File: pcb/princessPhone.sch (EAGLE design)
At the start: 78 parts, among them P1 TC2030-MCP-NL, P2 10118194, P3 95009-7441, Q1 2N7002K, U1 Value, U2 AG1170-S3-VERTICAL, U3 PI32MX170D-PT, U4 BLUETOOTH-RN-52

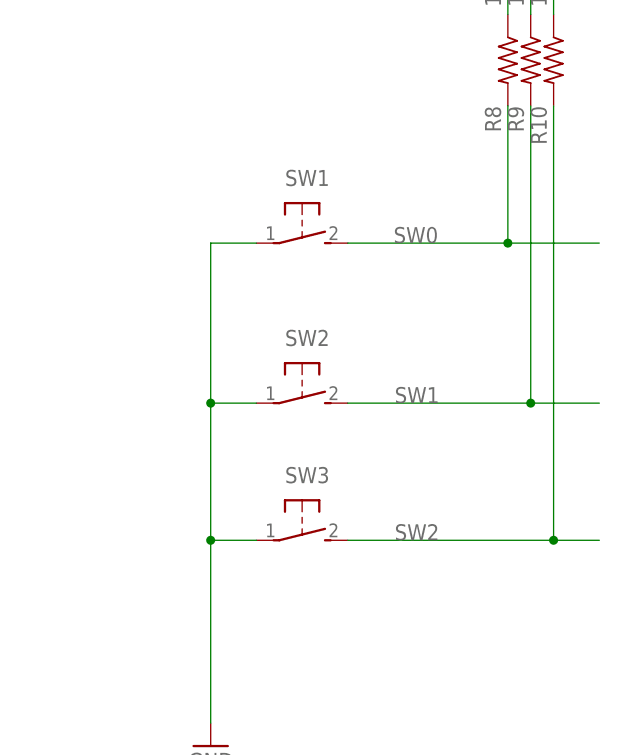
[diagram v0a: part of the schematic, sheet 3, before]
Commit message: Replaced placeholder components with proper ones.
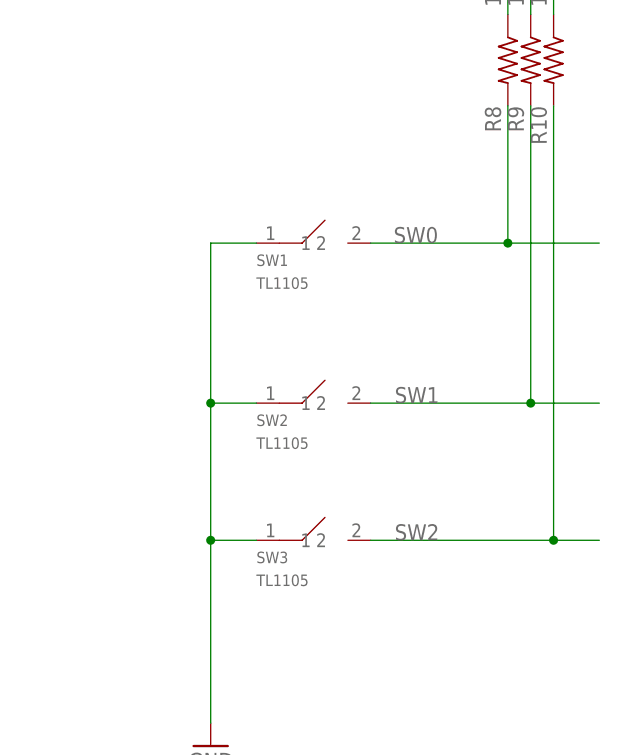
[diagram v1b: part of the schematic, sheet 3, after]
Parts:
- C1, C3: device rcl:CPOL-US153CLV-0505 -> rcl:CPOL-USE2.5-7
- SW1, SW2, SW3: value (none) -> TL1105; device switch-omron:31-XX -> princessPhone:TL1105
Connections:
- net GND: now also SW1.1, SW2.1, SW3.1; no longer SW1.P, SW2.P, SW3.P
- net SW0: now also SW1.2; no longer SW1.S
- net SW1: now also SW2.2; no longer SW2.S
- net SW2: now also SW3.2; no longer SW3.S
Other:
- note added: "2015.08.10"
- note added: "CORRECTED A FEW DRC ERRORS, REPLACED BIG CAPS AND BUTTONS"
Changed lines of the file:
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@@
 <part name="+3V31" library="supply1" deviceset="+3V3" device=""/>
 <part name="GND1" library="supply1" deviceset="GND" device=""/>
-<part name="C1" library="rcl" deviceset="CPOL-US" device="153CLV-0505" value="220UF"/>
+<part name="C1" library="rcl" deviceset="CPOL-US" device="E2.5-7" value="220UF"/>
 <part name="C2" library="rcl" deviceset="C-US" device="C0603" value="0.1UF"/>
 <part name="R1" library="rcl" deviceset="R-US_" device="R0603" value="2"/>
-<part name="C3" library="rcl" deviceset="CPOL-US" device="153CLV-0505" value="100UF"/>
+<part name="C3" library="rcl" deviceset="CPOL-US" device="E2.5-7" value="100UF"/>
 <part name="C4" library="rcl" deviceset="C-US" device="C0603" value="0.1UF"/>
 <part name="R2" library="rcl" deviceset="R-US_" device="R0603" value="1K"/>
@@
 <part name="LED4" library="led" deviceset="LED" device="CHIPLED_0603" value="BLUE"/>
 <part name="R29" library="rcl" deviceset="R-US_" device="R0603" value="150"/>
-<part name="SW1" library="switch-omron" deviceset="31-XX" device=""/>
-<part name="SW2" library="switch-omron" deviceset="31-XX" device=""/>
-<part name="SW3" library="switch-omron" deviceset="31-XX" device=""/>
 <part name="P2" library="console_board" deviceset="10118194" device=""/>
 <part name="P3" library="princessPhone" deviceset="95009-7441" device=""/>
+<part name="SW1" library="princessPhone" deviceset="TL1105*" device=""/>
+<part name="SW2" library="princessPhone" deviceset="TL1105*" device=""/>
+<part name="SW3" library="princessPhone" deviceset="TL1105*" device=""/>
 </parts>
 <sheets>
@@
 <text x="144.78" y="165.1" size="2.54" layer="94">2015.08.09</text>
 <text x="193.04" y="165.1" size="2.54" layer="94">FINISHED ROUTING, UPDATED USB/RJ-11/BOARD OUTLINE</text>
+<text x="50.8" y="160.02" size="2.54" layer="94">ANDERS NELSON</text>
+<text x="144.78" y="160.02" size="2.54" layer="94">2015.08.10</text>
+<text x="193.04" y="154.94" size="2.54" layer="94">CORRECTED A FEW DRC ERRORS,
+REPLACED BIG CAPS AND BUTTONS</text>
 </plain>
 <instances>
@@
 <attribute name="VALUE" x="149.86" y="33.02" size="1.778" layer="96"/>
 </instance>
-<instance part="SW1" gate="1" x="322.58" y="149.86" rot="R270"/>
-<instance part="SW2" gate="1" x="322.58" y="132.08" rot="R270"/>
-<instance part="SW3" gate="1" x="322.58" y="116.84" rot="R270"/>
+<instance part="SW1" gate="G$1" x="322.58" y="149.86"/>
+<instance part="SW2" gate="G$1" x="322.58" y="132.08"/>
+<instance part="SW3" gate="G$1" x="322.58" y="116.84"/>
 </instances>
 <busses>
@@
 <junction x="312.42" y="132.08"/>
 <pinref part="GND6" gate="1" pin="GND"/>
-<pinref part="SW1" gate="1" pin="P"/>
-<pinref part="SW2" gate="1" pin="P"/>
-<pinref part="SW3" gate="1" pin="P"/>
+<pinref part="SW1" gate="G$1" pin="1"/>
+<pinref part="SW2" gate="G$1" pin="1"/>
+<pinref part="SW3" gate="G$1" pin="1"/>
 </segment>
 </net>
@@
 <net name="SW0" class="0">
 <segment>
-<wire x1="327.66" y1="149.86" x2="345.44" y2="149.86" width="0.1524" layer="91"/>
+<wire x1="330.2" y1="149.86" x2="345.44" y2="149.86" width="0.1524" layer="91"/>
 <wire x1="345.44" y1="149.86" x2="355.6" y2="149.86" width="0.1524" layer="91"/>
 <wire x1="345.44" y1="165.1" x2="345.44" y2="149.86" width="0.1524" layer="91"/>
@@
 <label x="332.74" y="149.86" size="1.778" layer="95"/>
 <pinref part="R8" gate="G$1" pin="2"/>
-<pinref part="SW1" gate="1" pin="S"/>
+<pinref part="SW1" gate="G$1" pin="2"/>
 </segment>
 <segment>
@@
 <net name="SW1" class="0">
 <segment>
-<wire x1="327.66" y1="132.08" x2="347.98" y2="132.08" width="0.1524" layer="91"/>
+<wire x1="330.2" y1="132.08" x2="347.98" y2="132.08" width="0.1524" layer="91"/>
 <wire x1="347.98" y1="132.08" x2="355.6" y2="132.08" width="0.1524" layer="91"/>
 <wire x1="347.98" y1="165.1" x2="347.98" y2="132.08" width="0.1524" layer="91"/>
@@
 <label x="337.82" y="132.08" size="1.778" layer="95" rot="MR0"/>
 <pinref part="R9" gate="G$1" pin="2"/>
-<pinref part="SW2" gate="1" pin="S"/>
+<pinref part="SW2" gate="G$1" pin="2"/>
 </segment>
 <segment>
@@
 <net name="SW2" class="0">
 <segment>
-<wire x1="327.66" y1="116.84" x2="350.52" y2="116.84" width="0.1524" layer="91"/>
+<wire x1="330.2" y1="116.84" x2="350.52" y2="116.84" width="0.1524" layer="91"/>
 <wire x1="350.52" y1="116.84" x2="355.6" y2="116.84" width="0.1524" layer="91"/>
 <wire x1="350.52" y1="165.1" x2="350.52" y2="116.84" width="0.1524" layer="91"/>
@@
 <label x="337.82" y="116.84" size="1.778" layer="95" rot="MR0"/>
 <pinref part="R10" gate="G$1" pin="2"/>
-<pinref part="SW3" gate="1" pin="S"/>
-</segment>
-<segment>
+<pinref part="SW3" gate="G$1" pin="2"/>
+</segment>
+<segment>

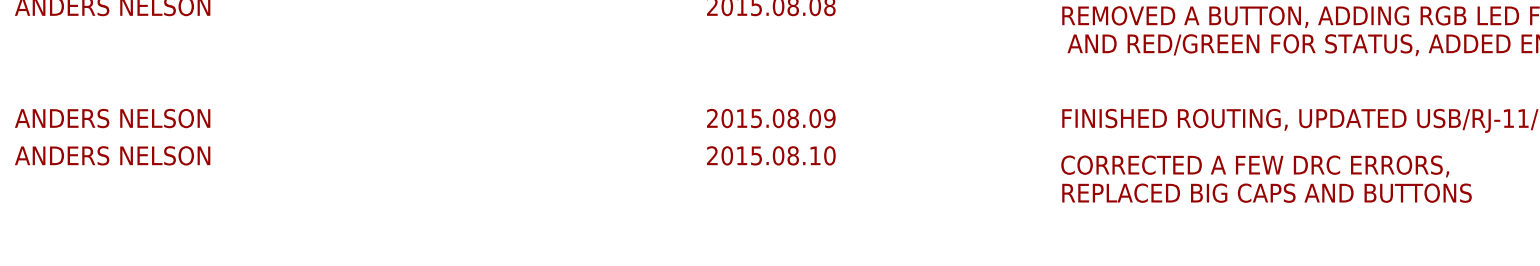
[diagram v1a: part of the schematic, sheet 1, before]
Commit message: Synced package sizes.
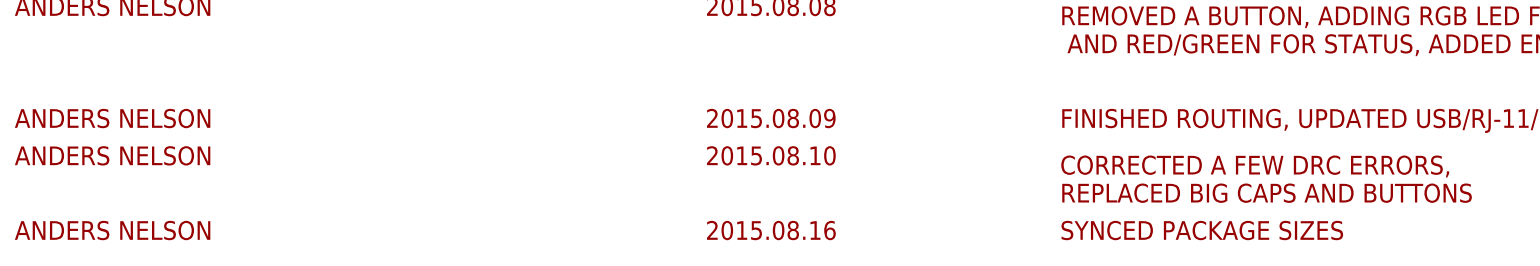
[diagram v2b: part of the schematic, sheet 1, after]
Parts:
- C10, C7, C8: device rcl:C-USC0402 -> rcl:C-USC0603
- C5: device rcl:C-USC0805 -> rcl:C-USC0603
- R14, R15, R5, R6, R7: device rcl:R-US_R0402 -> rcl:R-US_R0603
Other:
- note added: "2015.08.16"
- note added: "SYNCED PACKAGE SIZES"
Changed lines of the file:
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@@
 <part name="R2" library="rcl" deviceset="R-US_" device="R0603" value="1K"/>
 <part name="U2" library="princessPhone" deviceset="AG1170*" device="-VERTICAL" technology="-S3"/>
-<part name="C8" library="rcl" deviceset="C-US" device="C0402" value="0.1UF"/>
-<part name="C7" library="rcl" deviceset="C-US" device="C0402" value="1UF"/>
+<part name="C8" library="rcl" deviceset="C-US" device="C0603" value="0.1UF"/>
+<part name="C7" library="rcl" deviceset="C-US" device="C0603" value="1UF"/>
 <part name="C9" library="rcl" deviceset="C-US" device="C0603" value="10UF"/>
 <part name="GND5" library="supply1" deviceset="GND" device=""/>
-<part name="C10" library="rcl" deviceset="C-US" device="C0402" value="0.1UF"/>
-<part name="R5" library="rcl" deviceset="R-US_" device="R0402" value="10K"/>
+<part name="C10" library="rcl" deviceset="C-US" device="C0603" value="0.1UF"/>
+<part name="R5" library="rcl" deviceset="R-US_" device="R0603" value="10K"/>
 <part name="+3V34" library="supply1" deviceset="+3V3" device=""/>
 <part name="P1" library="raveGearControl" deviceset="TC2030" device="-MCP-NL"/>
@@
 <part name="TP13" library="testpad" deviceset="PTR1" device="B1,27"/>
 <part name="TP14" library="testpad" deviceset="PTR1" device="B1,27"/>
-<part name="R6" library="rcl" deviceset="R-US_" device="R0402" value="10K"/>
-<part name="R7" library="rcl" deviceset="R-US_" device="R0402" value="10K"/>
+<part name="R6" library="rcl" deviceset="R-US_" device="R0603" value="10K"/>
+<part name="R7" library="rcl" deviceset="R-US_" device="R0603" value="10K"/>
 <part name="+3V35" library="supply1" deviceset="+3V3" device=""/>
 <part name="U4" library="SparkFun-RF" deviceset="BLUETOOTH-RN-52" device=""/>
 <part name="FRAME4" library="frames" deviceset="FRAME_B_L" device=""/>
-<part name="C5" library="rcl" deviceset="C-US" device="C0805" value="10UF"/>
+<part name="C5" library="rcl" deviceset="C-US" device="C0603" value="10UF"/>
 <part name="C6" library="rcl" deviceset="C-US" device="C1206" value="22UF"/>
 <part name="GND2" library="supply1" deviceset="GND" device=""/>
@@
 <part name="GND10" library="supply1" deviceset="GND" device=""/>
 <part name="GND11" library="supply1" deviceset="GND" device=""/>
-<part name="R14" library="rcl" deviceset="R-US_" device="R0402" value="0"/>
-<part name="R15" library="rcl" deviceset="R-US_" device="R0402" value="0"/>
+<part name="R14" library="rcl" deviceset="R-US_" device="R0603" value="0"/>
+<part name="R15" library="rcl" deviceset="R-US_" device="R0603" value="0"/>
 <part name="R16" library="rcl" deviceset="R-US_" device="R0603" value="0"/>
 <part name="R17" library="rcl" deviceset="R-US_" device="R0603" value="0"/>
@@
 <text x="193.04" y="154.94" size="2.54" layer="94">CORRECTED A FEW DRC ERRORS,
 REPLACED BIG CAPS AND BUTTONS</text>
+<text x="50.8" y="149.86" size="2.54" layer="94">ANDERS NELSON</text>
+<text x="144.78" y="149.86" size="2.54" layer="94">2015.08.16</text>
+<text x="193.04" y="149.86" size="2.54" layer="94">SYNCED PACKAGE SIZES</text>
 </plain>
 <instances>

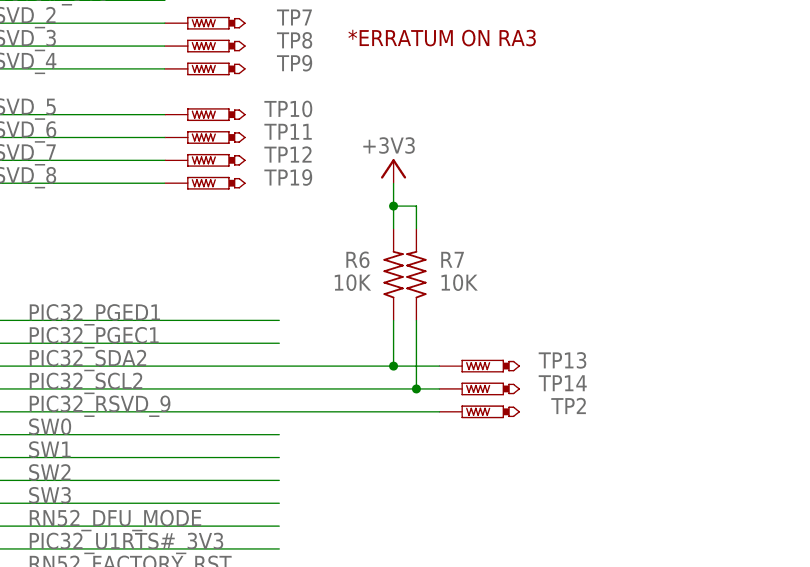
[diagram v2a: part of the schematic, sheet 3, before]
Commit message: Post-fab PCB tweaks.
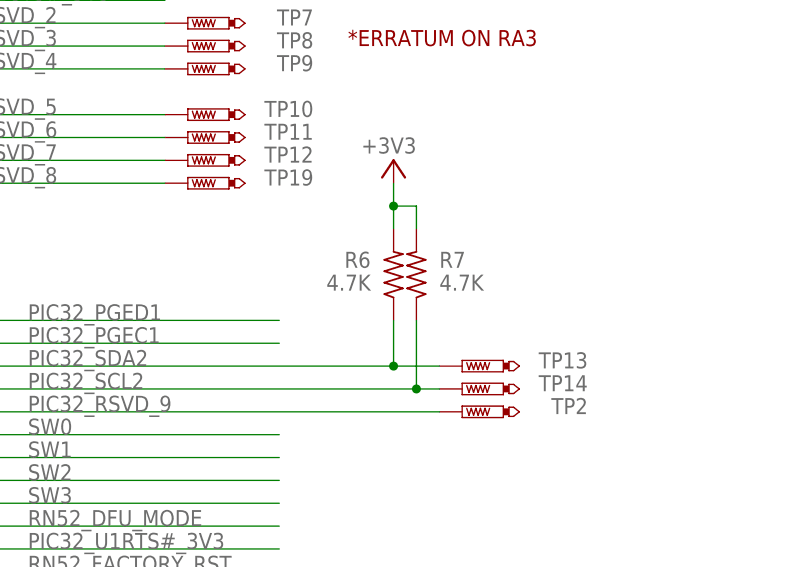
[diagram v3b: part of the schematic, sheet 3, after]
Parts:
- R6, R7: value 10K -> 4.7K
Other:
- note added: "1. CHANGE TO 6-PIN RJ-11 JACK"
- note added: "2. ENLARGE THROUGH-HOLES FOR AG1170"
- note added: "2015.09.01"
- note added: "ADDED TODO NOTES"
- note added: "TODO:"
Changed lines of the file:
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@@
 <part name="TP13" library="testpad" deviceset="PTR1" device="B1,27"/>
 <part name="TP14" library="testpad" deviceset="PTR1" device="B1,27"/>
-<part name="R6" library="rcl" deviceset="R-US_" device="R0603" value="10K"/>
-<part name="R7" library="rcl" deviceset="R-US_" device="R0603" value="10K"/>
+<part name="R6" library="rcl" deviceset="R-US_" device="R0603" value="4.7K"/>
+<part name="R7" library="rcl" deviceset="R-US_" device="R0603" value="4.7K"/>
 <part name="+3V35" library="supply1" deviceset="+3V3" device=""/>
 <part name="U4" library="SparkFun-RF" deviceset="BLUETOOTH-RN-52" device=""/>
@@
 <text x="144.78" y="149.86" size="2.54" layer="94">2015.08.16</text>
 <text x="193.04" y="149.86" size="2.54" layer="94">SYNCED PACKAGE SIZES</text>
+<text x="50.8" y="144.78" size="2.54" layer="94">ANDERS NELSON</text>
+<text x="144.78" y="144.78" size="2.54" layer="94">2015.09.01</text>
+<text x="193.04" y="144.78" size="2.54" layer="94">ADDED TODO NOTES</text>
 </plain>
 <instances>
@@
 <text x="261.62" y="226.06" size="2.54" layer="94">3. PIC32MX170 = 30mA</text>
 <text x="261.62" y="220.98" size="2.54" layer="94">4. LEDS = 10mA * 4 = 40mA</text>
+<text x="309.88" y="99.06" size="2.54" layer="94">TODO:</text>
+<text x="309.88" y="93.98" size="2.54" layer="94">1. CHANGE TO 6-PIN RJ-11 JACK</text>
+<text x="309.88" y="88.9" size="2.54" layer="94">2. ENLARGE THROUGH-HOLES FOR AG1170</text>
 </plain>
 <instances>
